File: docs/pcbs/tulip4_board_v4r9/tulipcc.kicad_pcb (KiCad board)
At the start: 2 copper layers, 134 x 88 mm, 101 parts, among them J1 XF2M-4015-1A, J2 1734709-4, J3 217179-0001, J4 SJ2-35863B1, J5 217179-0001, J6 SJ2-35863B1, J7 SJ2-35863B1, J8 1734827-2, Q1 DMP3099L, SW1 JS102011JAQN, U1 ESP32-S3-WROOM-2-N32R8V, U10 MCP73832, U11 MAX17048G, U12 TPS7A4533DCQR, U13 MIC2875-5.0YMT, U2 MBT3904DW1T1G, U3 USBLC6-2SC6, U4 FT231XS, U5 MIC2005A-2YM5-TR, U6 H11L1SR2M, U7 USBLC6-2SC6, U8 PCM5101A-Q1, U9 TPA6110A2DGN

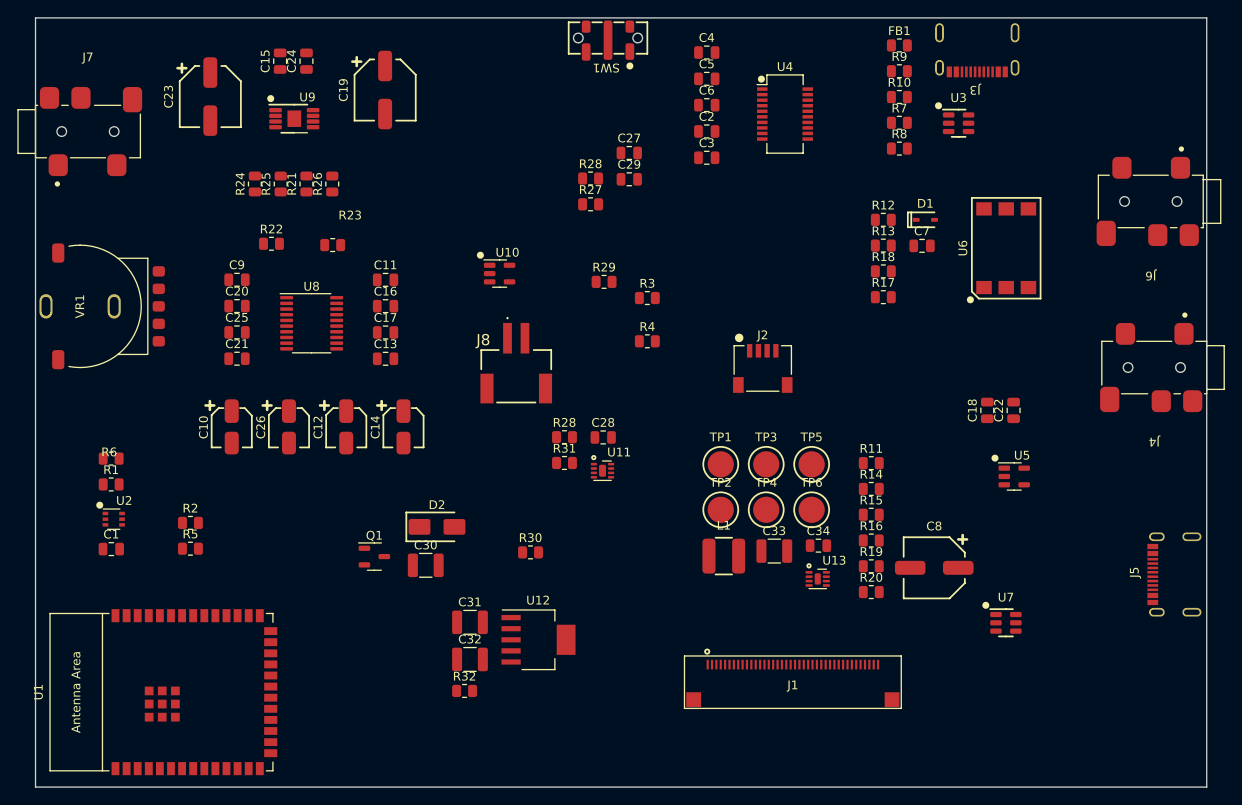
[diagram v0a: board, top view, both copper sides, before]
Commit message: Board outline + mounting holes
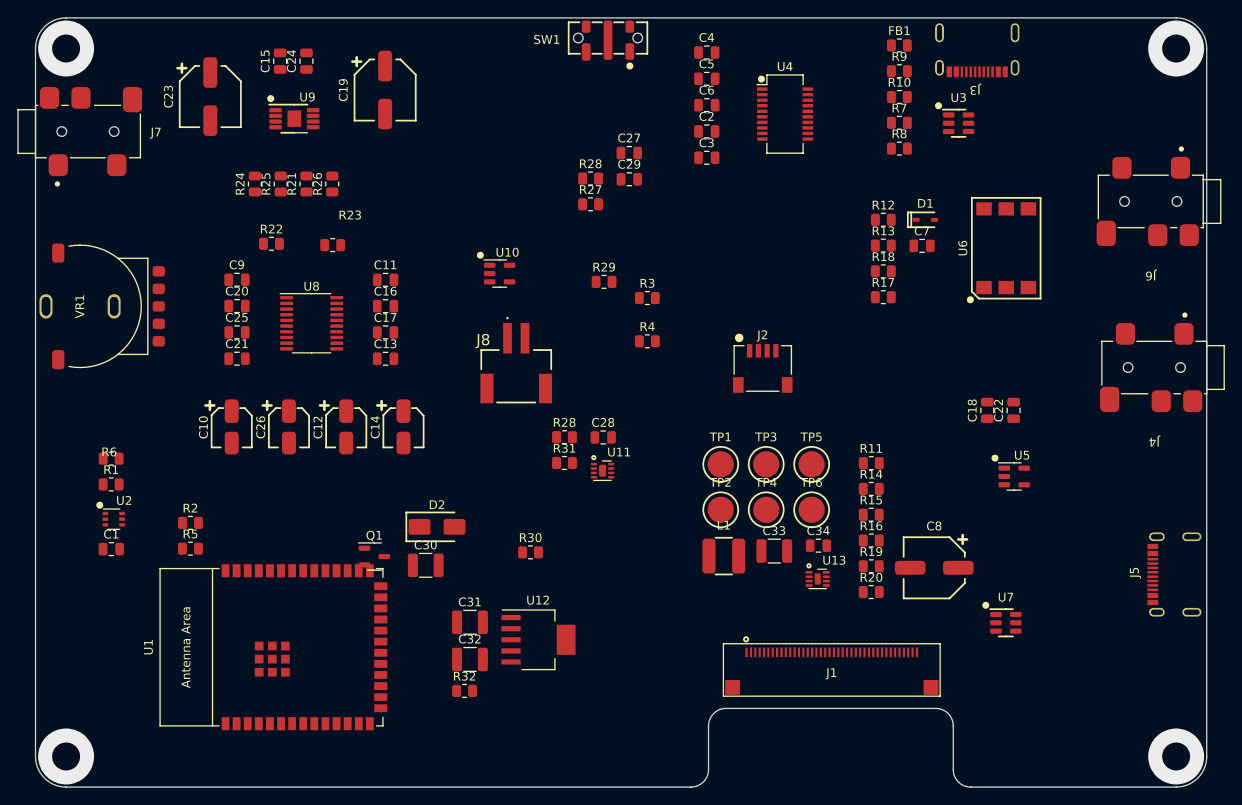
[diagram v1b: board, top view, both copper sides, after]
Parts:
- moved U1 13.6 mm to (30.0, -16.0)
- moved J1 4.67 mm to (91.1, -15.0)
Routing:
- net (no net): vias 0 -> 4
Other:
- outline, holes or cut-outs redrawn
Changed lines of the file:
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@@
     (property "ki_description" "Slide switch SMD, right angle, single pole dual throw")
     (attr smd)
-    (fp_text reference "SW1" (at 0.2 -3.4 180 unlocked) (layer "F.SilkS")
+    (fp_text reference "SW1" (at 7 -0.2 unlocked) (layer "F.SilkS")
         (effects (font (size 1 1) (thickness 0.15)))
     )
-    (fp_text value "JS102011JAQN" (at 0.1 2.8 180 unlocked) (layer "F.Fab")
+    (fp_text value "JS102011JAQN" (at 0.1 -3.7 unlocked) (layer "F.Fab")
         (effects (font (size 1 1) (thickness 0.15)))
     )
-    (fp_text user "${REFERENCE}" (at 0 4.3 180 unlocked) (layer "F.Fab")
+    (fp_text user "${REFERENCE}" (at 7 -0.2 unlocked) (layer "F.Fab")
         (effects (font (size 1 1) (thickness 0.15)))
     )
@@
     (property "ki_description" "Audio 3.5mm connector TRS Tip Switch")
     (attr smd)
-    (fp_text reference "J7" (at 0 -8.5 unlocked) (layer "F.SilkS")
+    (fp_text reference "J7" (at 7.8 0.1 unlocked) (layer "F.SilkS")
         (effects (font (size 1 1) (thickness 0.15)))
     )
@@
   )
   (footprint "tulipcc_footprint_lib:OMRON_XF2M-4015-1A" (layer "F.Cu")
-    (at 86.65 -13.6)
+    (at 91.1 -15)
     (property "Manufacturer" "Omron")
     (property "Part #" "XF2M-4015-1A")
@@
   )
   (footprint "tulipcc_footprint_lib:ESP32-S3-WROOM-2" (layer "F.Cu")
-    (at 17.41 -10.86 90)
+    (at 30 -16 90)
     (descr "ESP32-S3-WROOM-2 is a powerful, generic Wi-Fi + Bluetooth LE MCU modules that have Dual core CPU , a rich set of peripherals, provides acceleration for neural network computing and signal processing workloads. They are an ideal choice for a wide variety of application scenarios related to AI + Internet of Things (AIoT), such as wake word detection and speech commands recognition , face detection and recognition, smart home, smart appliance, smart control panel, smart speaker etc.")
     (tags "esp32-s3")
@@
     )
   )
-  (gr_rect (start 0 -88) (end 134 0)
-    (stroke (width 0.1) (type default)) (fill none) (layer "Edge.Cuts"))
+  (gr_arc (start 77 -2) (mid 76.414214 -0.585786) (end 75 0)
+    (stroke (width 0.1) (type default)) (layer "Edge.Cuts"))
+  (gr_arc (start 77 -7) (mid 77.585786 -8.414214) (end 79 -9)
+    (stroke (width 0.1) (type default)) (layer "Edge.Cuts"))
+  (gr_line (start 134 -3.5) (end 134 -84.5)
+    (stroke (width 0.1) (type default)) (layer "Edge.Cuts"))
+  (gr_line (start 0 -84.5) (end 0 -3.5)
+    (stroke (width 0.1) (type default)) (layer "Edge.Cuts"))
+  (gr_line (start 79 -9) (end 103 -9)
+    (stroke (width 0.1) (type default)) (layer "Edge.Cuts"))
+  (gr_arc (start 134 -3.5) (mid 132.974874 -1.025126) (end 130.5 0)
+    (stroke (width 0.1) (type default)) (layer "Edge.Cuts"))
+  (gr_arc (start 107 0) (mid 105.585786 -0.585786) (end 105 -2)
+    (stroke (width 0.1) (type default)) (layer "Edge.Cuts"))
+  (gr_line (start 107 0) (end 130.5 0)
+    (stroke (width 0.1) (type default)) (layer "Edge.Cuts"))
+  (gr_arc (start 130.5 -88) (mid 132.974874 -86.974874) (end 134 -84.5)
+    (stroke (width 0.1) (type default)) (layer "Edge.Cuts"))
+  (gr_arc (start 0 -84.5) (mid 1.025126 -86.974874) (end 3.5 -88)
+    (stroke (width 0.1) (type default)) (layer "Edge.Cuts"))
+  (gr_line (start 3.5 0) (end 75 0)
+    (stroke (width 0.1) (type default)) (layer "Edge.Cuts"))
+  (gr_arc (start 3.5 0) (mid 1.025126 -1.025126) (end 0 -3.5)
+    (stroke (width 0.1) (type default)) (layer "Edge.Cuts"))
+  (gr_arc (start 103 -9) (mid 104.414214 -8.414214) (end 105 -7)
+    (stroke (width 0.1) (type default)) (layer "Edge.Cuts"))
+  (gr_line (start 77 -2) (end 77 -7)
+    (stroke (width 0.1) (type default)) (layer "Edge.Cuts"))
+  (gr_line (start 105 -2) (end 105 -7)
+    (stroke (width 0.1) (type default)) (layer "Edge.Cuts"))
+  (gr_line (start 3.5 -88) (end 130.5 -88)
+    (stroke (width 0.1) (type default)) (layer "Edge.Cuts"))
+  (via (at 3.5 -3.5) (size 6.4) (drill 3.2) (layers "F.Cu" "B.Cu") (net 0))
+  (via (at 3.5 -84.5) (size 6.4) (drill 3.2) (layers "F.Cu" "B.Cu") (net 0))
+  (via (at 130.5 -3.5) (size 6.4) (drill 3.2) (layers "F.Cu" "B.Cu") (net 0))
+  (via (at 130.5 -84.5) (size 6.4) (drill 3.2) (layers "F.Cu" "B.Cu") (net 0))
 )

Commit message: Progress routing
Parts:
- added C1: 0.1uF, tulipcc_footprint_lib:C_0805_2012, F.Cu at (54.0, -118.0)
- added C2: 22uF, tulipcc_footprint_lib:C_1210_3225, F.Cu at (54.6, -121.6)
- moved C20 145.9 mm to (-32.0, -81.0)
- moved C24 145.9 mm to (-29.0, -81.0)
- moved C4 134.0 mm to (-42.0, -13.0)
- moved C5 134.0 mm to (-42.0, -10.0)
- moved SW1 121.5 mm to (37.5, 32.5), turned to -90 degrees
- moved J3 120.4 mm to (2.80, -26.0), turned to -90 degrees
- moved TP3 115.1 mm to (172.8, 35.8)
- moved TP4 115.1 mm to (172.8, 41.0)
- moved TP1 115.1 mm to (167.6, 35.8)
- moved TP2 115.1 mm to (167.6, 41.0)
- moved TP5 115.1 mm to (178.0, 35.8)
- moved TP6 115.1 mm to (178.0, 41.0)
- moved C3 107.6 mm to (90.0, -97.6)
- moved R1 107.6 mm to (90.0, -105.0)
- moved R2 107.6 mm to (99.1, -100.6)
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- renumbered C8 to C10, C9 to C11, C10 to C12, C11 to C13, C12 to C14, C13 to C15, C14 to C16, C15 to C17, C16 to C18, C17 to C19, C18 to C20, C19 to C21, C20 to C22, C21 to C23, C22 to C24, C23 to C25, C24 to C26, C25 to C27, C26 to C28, C27 to C29, C1 to C3, C28 to C30, C29 to C31, C30 to C32, C31 to C33, C32 to C34, C33 to C35, C34 to C36, C2 to C4, C3 to C5, C4 to C6, C5 to C7, C6 to C8, C7 to C9
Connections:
- U7 pad 5: +5V -> +5VL
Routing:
- net UART0_RXD: track 0.00 -> 128.6 mm, vias 0 -> 2
- net UART0_TXD: track 0.00 -> 119.9 mm, vias 0 -> 2
- net LCD_DE: track 0.00 -> 95.5 mm, vias 0 -> 2
- net LCD_VSYNC: track 0.00 -> 89.8 mm, vias 0 -> 2
- net LCD_HSYNC: track 0.00 -> 86.5 mm, vias 0 -> 2
- net LCD_BLEN: track 0.00 -> 80.7 mm, vias 0 -> 2
- net +3.3V: track 0.00 -> 78.1 mm, vias 0 -> 4
- net USB_D-: track 0.00 -> 75.3 mm
- net USB_D+: track 0.00 -> 73.3 mm
- net LCD_R5: track 0.00 -> 68.4 mm, vias 0 -> 2
- net LCD_PCLK: track 0.00 -> 67.0 mm, vias 0 -> 2
- net LCD_B7: track 0.00 -> 66.1 mm, vias 0 -> 2
- net LCD_R6: track 0.00 -> 65.9 mm, vias 0 -> 2
- net LCD_R7: track 0.00 -> 64.1 mm, vias 0 -> 2
- net LCD_INT: track 0.00 -> 61.8 mm, vias 0 -> 2
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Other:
- outline, holes or cut-outs redrawn
- board text added: "CHARGE SERIAL"
- board text added: "LCD"
- board text added: "MIDI IN"
- board text added: "MIDI OUT"
- board text added: "USB HOST"

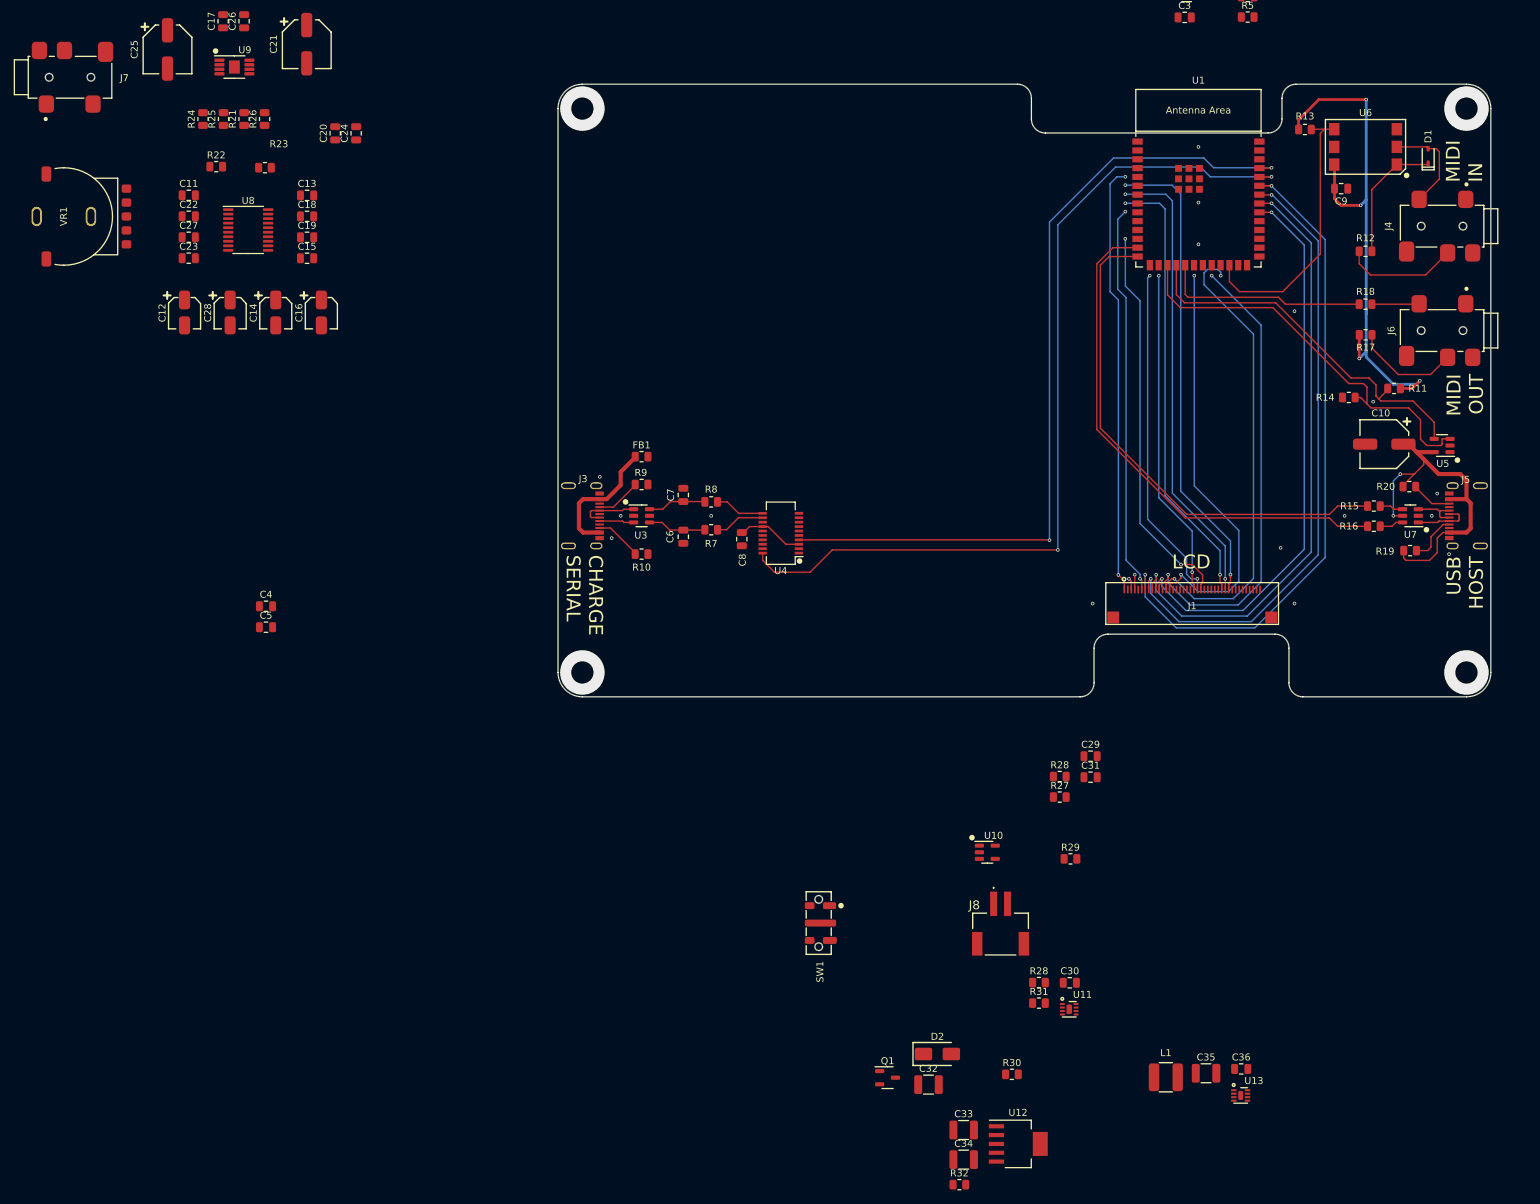
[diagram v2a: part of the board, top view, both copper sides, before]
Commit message: Progress routing PCB
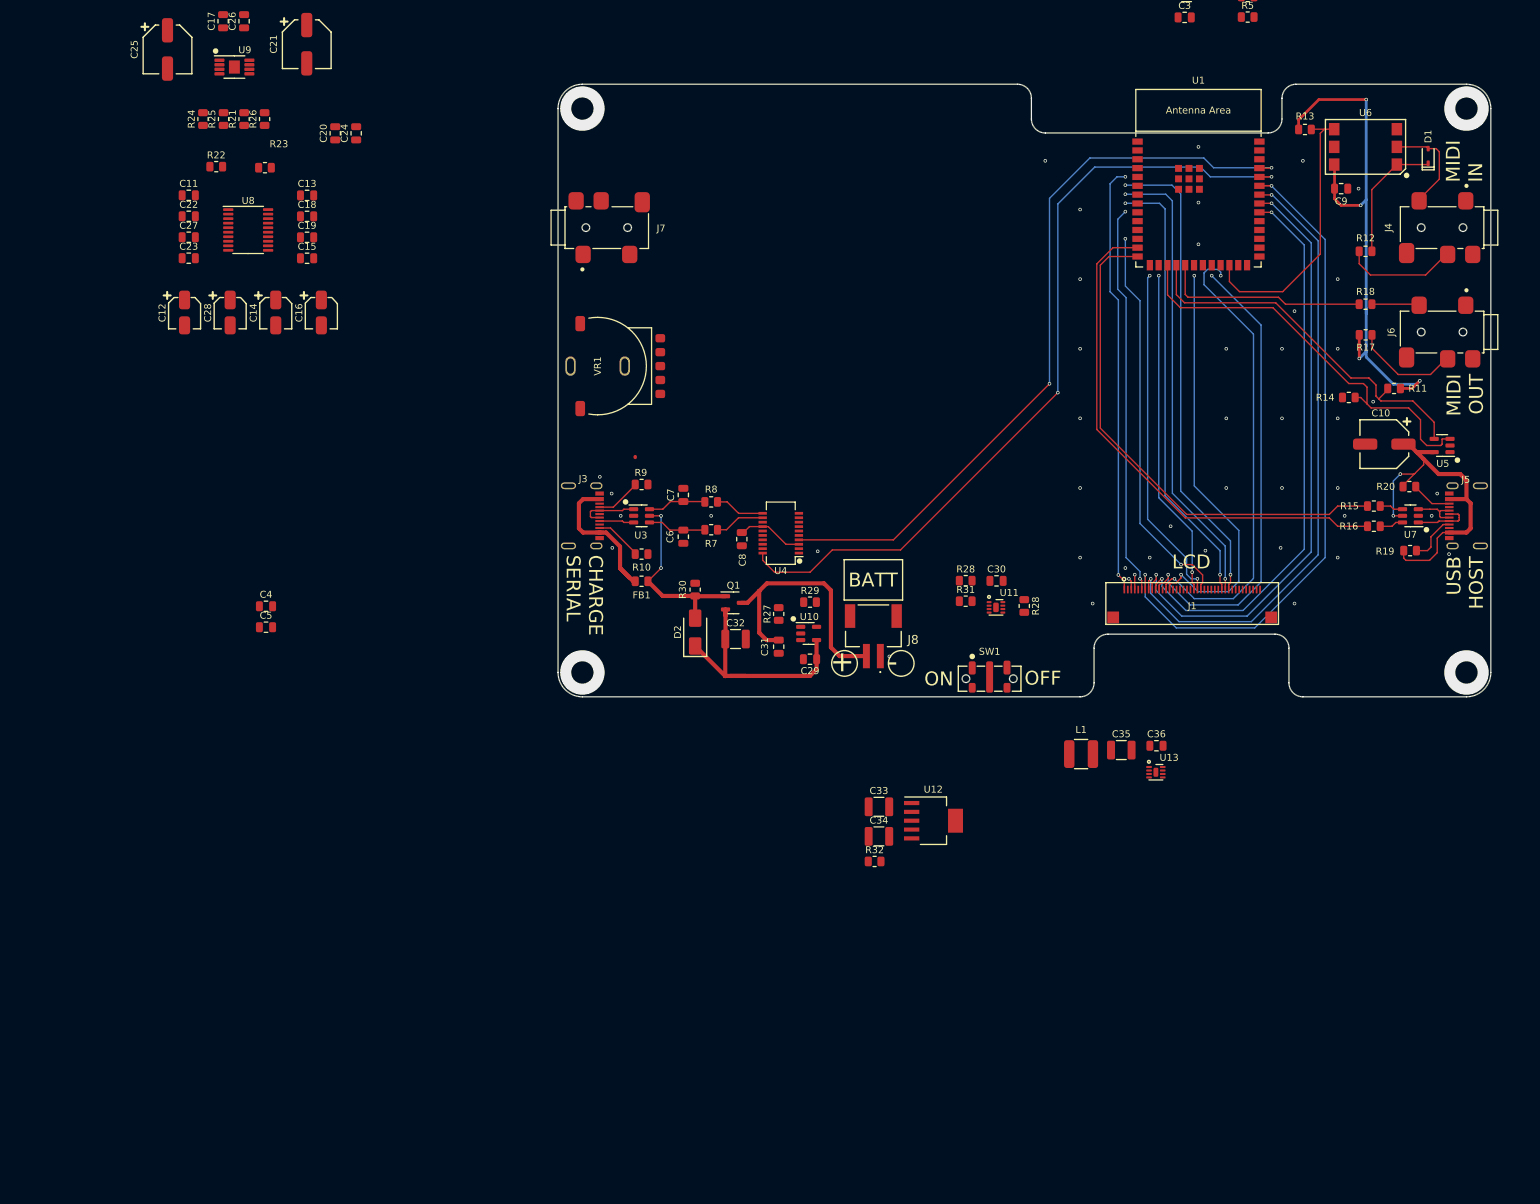
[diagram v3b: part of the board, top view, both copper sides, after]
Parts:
- moved R30 83.2 mm to (19.7, -15.4), turned to -90 degrees
- moved J7 80.1 mm to (7.00, -67.4)
- moved VR1 79.6 mm to (5.69, -47.5)
- moved Q1 71.7 mm to (25.2, -13.5)
- moved D2 69.9 mm to (19.7, -9.30), turned to 90 degrees
- moved C32 69.8 mm to (25.5, -8.30)
- moved C30 58.7 mm to (63.0, -16.7)
- moved R28 58.7 mm to (58.6, -16.7)
- moved R31 58.7 mm to (58.6, -13.7)
- moved U11 58.7 mm to (62.9, -12.8)
- moved R29 52.5 mm to (36.2, -13.6)
- moved C31 48.6 mm to (31.7, -7.20), turned to -90 degrees
- moved R27 48.2 mm to (31.7, -11.9), turned to 90 degrees
- moved C34 48.0 mm to (46.1, 20.1)
- moved C35 48.0 mm to (80.9, 7.65)
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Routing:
- net +BATT: track 0.00 -> 37.5 mm
- net +VSW: track 0.00 -> 36.5 mm
- net VBUS: track 0.00 -> 27.1 mm, vias 0 -> 2
- net UART0_RXD: track 128.6 -> 117.2 mm
- net UART0_TXD: track 119.9 -> 108.6 mm
- net Net-(FB1-Pad1): track 19.1 -> 22.2 mm
- net GND: vias 16 -> 43
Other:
- board text added: "+"
- board text added: "-"
- board text added: "BATT"
- board text added: "OFF"
- board text added: "ON"

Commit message: Routing complete
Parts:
- removed the R28 at (58.6, -16.7)
- removed the R28 at (67.0, -13.0)
- added G***: LOGO, LOGO, F.Cu at (91.8, -50.9)
- added R28: 10K, tulipcc_footprint_lib:R_0805_2012, F.Cu at (58.0, -18.0)
- moved TP4 175.6 mm to (45.4, -79.9)
- moved TP6 172.3 mm to (55.2, -79.9)
- moved TP3 166.1 mm to (29.1, -47.6)
- moved TP1 161.4 mm to (11.7, -6.00)
- moved TP2 134.6 mm to (40.6, -3.60)
- moved C27 106.9 mm to (53.8, -63.4), turned to -90 degrees
- moved C28 106.4 mm to (58.7, -66.2), turned to -90 degrees
- moved C12 99.2 mm to (44.0, -72.2), turned to 0 degrees
- moved C11 97.4 mm to (44.2, -66.9), turned to 180 degrees
- moved J2 96.3 mm to (71.3, -14.6), turned to 0 degrees
- moved C22 93.4 mm to (40.1, -62.9), turned to 180 degrees
- moved C23 93.2 mm to (40.1, -65.4), turned to 180 degrees
- moved U8 92.9 mm to (48.2, -61.6)
- moved R1 91.3 mm to (44.3, -26.0), turned to -90 degrees
- moved R6 89.7 mm to (45.7, -30.0), turned to 180 degrees
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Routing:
- net +3.3V: track 78.1 -> 489.3 mm, vias 4 -> 18
- net +5V: track 0.00 -> 138.0 mm, vias 0 -> 5
- net CHARGE_STATE: track 0.00 -> 135.3 mm, vias 0 -> 4
- net I2C_SDA: track 2.09 -> 119.3 mm, vias 1 -> 6
- net I2C_SCL: track 1.68 -> 112.8 mm, vias 1 -> 6
- net +VSW: track 36.5 -> 128.6 mm, vias 0 -> 4
- net ESP32_BOOT: track 0.00 -> 86.2 mm, vias 0 -> 4
- net ESP32_EN: track 0.00 -> 83.8 mm, vias 0 -> 4
- net PCM_BCK: track 0.00 -> 69.9 mm, vias 0 -> 2
- net PCM_DIN: track 0.00 -> 66.8 mm, vias 0 -> 2
- net VREG_EN: track 0.00 -> 55.5 mm, vias 0 -> 2
- net Net-(U9-IN1-): track 0.00 -> 38.6 mm, vias 0 -> 2
- net PCM_LRCK: track 0.00 -> 38.5 mm
- net VBUS: track 27.1 -> 59.9 mm
- net Net-(U9-VO1): track 0.00 -> 29.1 mm
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- added copper zone on B.Cu, net GND
- added copper zone on F.Cu, net GND
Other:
- outline, holes or cut-outs redrawn
- board text added: "+3.3V"
- board text added: "+5V"
- board text added: "+VSW"
- board text added: "AUDIO OUT"
- board text added: "BATTERY"
- board text added: "COMPUTER"
- board text added: "CREATIVE"
- board text added: "GND"
- board text added: "I2C"
- board text added: "TULIP"
- board text added: "USB HOST POWER OUT"
- board text added: "USB SERIAL POWER IN"
- board text added: "V4R9"
- board text added: "VBUS"
- board text added: "VOLUME"
- board text removed: "BATT"
- board text removed: "CHARGE SERIAL"
- board text removed: "USB HOST"
